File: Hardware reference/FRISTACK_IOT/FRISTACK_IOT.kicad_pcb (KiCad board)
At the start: 2 copper layers, 51 x 51 mm, 66 parts, among them J1 MEM2075-00-140-01-A, J2 Conn_01x02_Pin, J3 Conn_01x13_Socket, J4 Conn_01x13_Socket, U1 TPS62840DLCR, U2 ESP32-C6-MINI-1-H4, U3 SN65HVD232, Y1 32.768 kHz

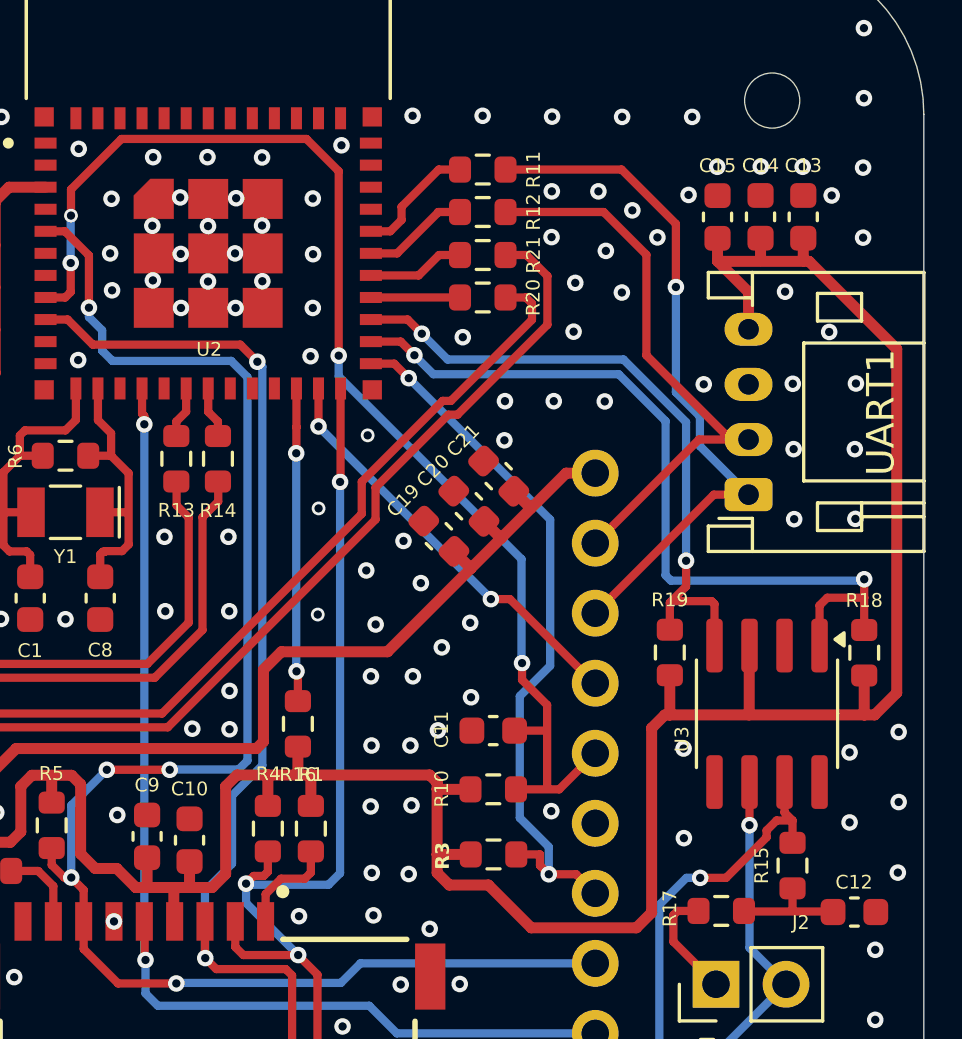
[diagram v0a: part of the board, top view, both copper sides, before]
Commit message: Added USBSwitch to Core and added first version of Compatibility
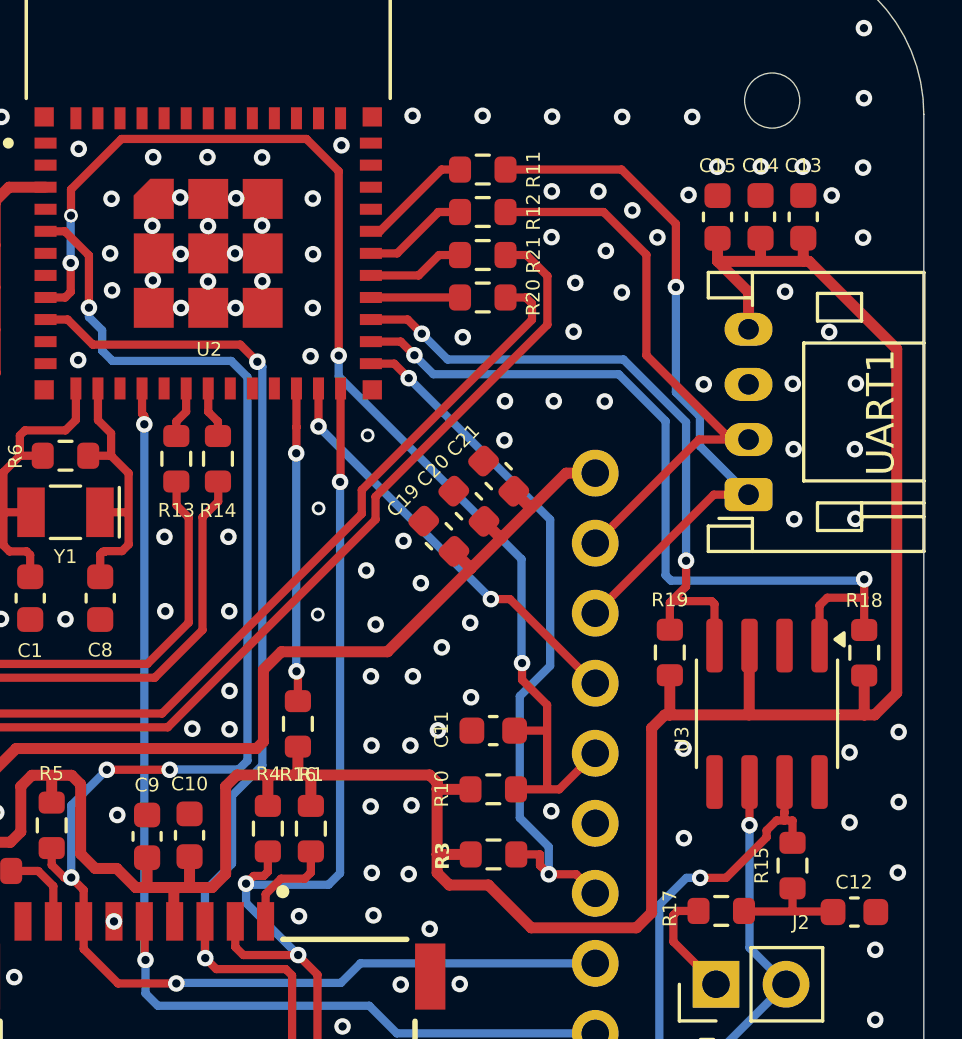
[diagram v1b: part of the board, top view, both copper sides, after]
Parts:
- moved C10 0.18 mm to (161.3, 98.1)
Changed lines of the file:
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@@
 			(psa4output no)
 			(plot_black_and_white yes)
-			(plotinvisibletext yes)
 			(sketchpadsonfab no)
 			(plotpadnumbers no)
@@
 	(footprint "Capacitor_SMD:C_0603_1608Metric"
 		(layer "F.Cu")
-		(at 161.28 98.255 90)
+		(at 161.28 98.075 90)
 		(descr "Capacitor SMD 0603 (1608 Metric), square (rectangular) end terminal, IPC_7351 nominal, (Body size source: IPC-SM-782 page 76, https://www.pcb-3d.com/wordpress/wp-content/uploads/ipc-sm-782a_amendment_1_and_2.pdf), generated with kicad-footprint-generator")
 		(tags "capacitor")
@@
 	)
 	(segment
-		(start 145.455 97.715)
-		(end 145.44 97.7)
-		(width 0.3)
-		(layer "F.Cu")
-		(net 12)
-	)
-	(segment
-		(start 170.76 82.32)
-		(end 173.7 79.38)
+		(start 147.945476 99.785349)
+		(end 154.071826 93.659)
 		(width 0.3)
 		(layer "F.Cu")
@@
 	)
 	(segment
-		(start 154.071826 93.659)
-		(end 160.28248 93.659)
+		(start 145.455 97.715)
+		(end 145.44 97.7)
 		(width 0.3)
 		(layer "F.Cu")
@@
 	)
 	(segment
-		(start 173.48 78.57)
-		(end 172.74 78.57)
+		(start 167.52574 86.41574)
+		(end 167.52574 85.55426)
 		(width 0.3)
 		(layer "F.Cu")
@@
 	)
 	(segment
-		(start 145.44 90.76)
-		(end 145.05 90.37)
-		(width 0.3)
-		(layer "F.Cu")
-		(net 12)
-	)
-	(segment
-		(start 167.52574 86.41574)
-		(end 167.52574 85.25426)
+		(start 167.52574 85.55426)
+		(end 173.7 79.38)
 		(width 0.3)
 		(layer "F.Cu")
@@
 	)
 	(segment
-		(start 147.945476 99.785349)
-		(end 154.071826 93.659)
+		(start 145.44 90.76)
+		(end 145.05 90.37)
 		(width 0.3)
 		(layer "F.Cu")
@@
 	)
 	(segment
-		(start 170.46 82.32)
-		(end 170.76 82.32)
+		(start 154.071826 93.659)
+		(end 160.28248 93.659)
 		(width 0.3)
 		(layer "F.Cu")
@@
 	)
 	(segment
-		(start 145.455 97.715)
-		(end 145.405 97.765)
+		(start 173.48 78.57)
+		(end 172.74 78.57)
 		(width 0.3)
 		(layer "F.Cu")
@@
 	)
 	(segment
-		(start 147.945476 100.18175)
-		(end 147.945476 99.785349)
+		(start 173.7 79.38)
+		(end 173.7 78.79)
 		(width 0.3)
 		(layer "F.Cu")
@@
 	)
 	(segment
-		(start 167.52574 85.25426)
-		(end 170.46 82.32)
+		(start 145.455 97.715)
+		(end 145.405 97.765)
 		(width 0.3)
 		(layer "F.Cu")
@@
 	)
 	(segment
-		(start 173.7 79.38)
-		(end 173.7 78.79)
+		(start 147.945476 100.18175)
+		(end 147.945476 99.785349)
 		(width 0.3)
 		(layer "F.Cu")
@@
 	)
 	(segment
-		(start 146.45 102.72)
-		(end 146.25 102.52)
+		(start 160.490001 94.16)
+		(end 168.02674 86.62326)
 		(width 0.3)
 		(layer "F.Cu")
@@
 	)
 	(segment
-		(start 170.999 82.821)
-		(end 174.26 79.56)
+		(start 146.45 102.72)
+		(end 146.25 102.52)
 		(width 0.3)
 		(layer "F.Cu")
@@
 	)
 	(segment
-		(start 168.02674 85.46178)
-		(end 170.66752 82.821)
+		(start 149.54 101.127226)
+		(end 149.54 98.899346)
 		(width 0.3)
 		(layer "F.Cu")
@@
 	)
 	(segment
-		(start 173.5 77.03)
-		(end 172.74 77.03)
-		(width 0.3)
-		(layer "F.Cu")
-		(net 18)
-	)
-	(segment
 		(start 147.945476 102.72175)
 		(end 147.943726 102.72)
@@
 	)
 	(segment
-		(start 168.02674 86.62326)
-		(end 168.02674 85.46178)
-		(width 0.3)
-		(layer "F.Cu")
-		(net 18)
-	)
-	(segment
-		(start 147.945476 102.72175)
-		(end 149.54 101.127226)
+		(start 154.279348 94.160001)
+		(end 160.490001 94.16)
 		(width 0.3)
 		(layer "F.Cu")
@@
 	)
 	(segment
-		(start 170.66752 82.821)
-		(end 170.999 82.821)
+		(start 146.44 102.71)
+		(end 146.44 89.59)
 		(width 0.3)
 		(layer "F.Cu")
@@
 	)
 	(segment
-		(start 149.54 101.127226)
-		(end 149.54 98.899346)
+		(start 149.54 98.899346)
+		(end 154.279345 94.160001)
 		(width 0.3)
 		(layer "F.Cu")
@@
 	)
 	(segment
-		(start 146.44 102.71)
-		(end 146.44 89.59)
+		(start 146.44 89.59)
+		(end 145.19 88.34)
 		(width 0.3)
 		(layer "F.Cu")
@@
 	)
 	(segment
-		(start 174.26 77.79)
-		(end 173.5 77.03)
+		(start 143.26155 88.34)
+		(end 143.23155 88.37)
 		(width 0.3)
 		(layer "F.Cu")
@@
 	)
 	(segment
-		(start 146.44 89.59)
-		(end 145.19 88.34)
+		(start 168.02674 85.79326)
+		(end 174.26 79.56)
 		(width 0.3)
 		(layer "F.Cu")
@@
 	)
 	(segment
-		(start 143.26155 88.34)
-		(end 143.23155 88.37)
+		(start 168.02674 86.62326)
+		(end 168.02674 85.79326)
 		(width 0.3)
 		(layer "F.Cu")
@@
 	)
 	(segment
-		(start 160.490001 94.16)
-		(end 168.02674 86.62326)
+		(start 174.26 77.79)
+		(end 173.5 77.03)
 		(width 0.3)
 		(layer "F.Cu")
@@
 	)
 	(segment
-		(start 149.54 98.899346)
-		(end 154.279345 94.160001)
+		(start 154.279345 94.160001)
+		(end 154.279349 94.16)
 		(width 0.3)
 		(layer "F.Cu")
@@
 	)
 	(segment
-		(start 154.279348 94.160001)
-		(end 160.490001 94.16)
+		(start 173.5 77.03)
+		(end 172.74 77.03)
 		(width 0.3)
 		(layer "F.Cu")
@@
 	)
 	(segment
-		(start 154.279345 94.160001)
-		(end 154.279349 94.16)
+		(start 147.945476 102.72175)
+		(end 149.54 101.127226)
 		(width 0.3)
 		(layer "F.Cu")
@@
 	)
 	(segment
-		(start 182.86 97.25)
-		(end 182.86 96.145)
-		(width 0.3)
-		(layer "F.Cu")
-		(net 20)
-	)
-	(segment
 		(start 182.57 97.54)
 		(end 182.21 97.9)
@@
 	)
 	(segment
+		(start 182.85 97.54)
+		(end 182.85 97.26)
+		(width 0.3)
+		(layer "F.Cu")
+		(net 20)
+	)
+	(segment
 		(start 182.21 98.15)
 		(end 180.74 99.62)
@@
 	)
 	(segment
+		(start 182.85 97.26)
+		(end 182.86 97.25)
+		(width 0.3)
+		(layer "F.Cu")
+		(net 20)
+	)
+	(segment
 		(start 180.74 99.62)
 		(end 179.8 99.62)
@@
 	)
 	(segment
-		(start 178.73 106.37)
-		(end 180.275 106.37)
+		(start 182.86 97.25)
+		(end 182.86 96.145)
 		(width 0.3)
 		(layer "F.Cu")
@@
 	)
 	(segment
-		(start 183.15 97.54)
-		(end 182.86 97.25)
+		(start 178.73 106.37)
+		(end 180.275 106.37)
 		(width 0.3)
 		(layer "F.Cu")
@@
 	)
 	(segment
-		(start 170.32 73.93)
-		(end 168.97 75.28)
-		(width 0.3)
-		(layer "F.Cu")
-		(net 29)
-	)
-	(segment
-		(start 168.5575 76.17)
+		(start 168.18 76.17)
 		(end 167.8575 76.17)
 		(width 0.3)
@@
 	)
 	(segment
-		(start 168.97 75.7575)
-		(end 168.5575 76.17)
-		(width 0.3)
-		(layer "F.Cu")
-		(net 29)
-	)
-	(segment
-		(start 168.97 75.28)
-		(end 168.97 75.7575)
+		(start 171.09 73.93)
+		(end 170.42 73.93)
 		(width 0.3)
 		(layer "F.Cu")
@@
 	)
 	(segment
-		(start 171.09 73.93)
-		(end 170.32 73.93)
+		(start 170.42 73.93)
+		(end 168.18 76.17)
 		(width 0.3)
 		(layer "F.Cu")
@@
 	)
 	(group ""
-		(members "2791a95b-42e5-4102-ae3b-9cf65cbf0bcc" "2dfbaade-4923-48d9-aa6f-134091588e89"
-			"31310593-05bf-4365-994b-4dc35888f404" "4e13a2d6-105e-4052-ba09-1d7e4f1ce143"
-			"88e18c7d-14a1-43d4-ac31-33f592af2c9c" "ee10c7a8-357f-46bc-b261-197f884fdc5f"
+		(members "2791a95b-42e5-4102-ae3b-9cf65cbf0bcc" "88e18c7d-14a1-43d4-ac31-33f592af2c9c"
+			"ee10c7a8-357f-46bc-b261-197f884fdc5f"
 		)
 	)

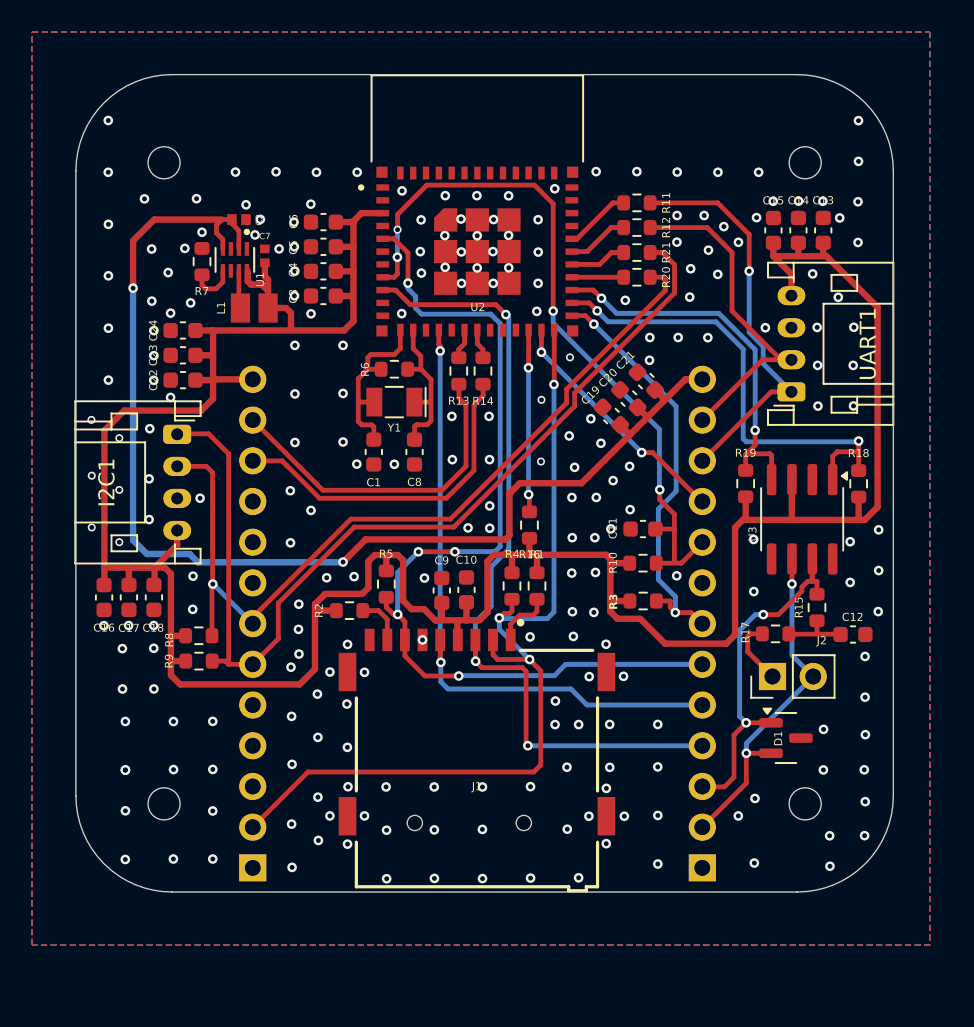
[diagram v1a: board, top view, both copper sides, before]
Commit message: review and new BATTERY board
IOT - changed twai termination from header to switch option, new holes , added power planes
SENSOR NODE - new holes and back silk text
CORE - vertical twai termination header changed to horizontal
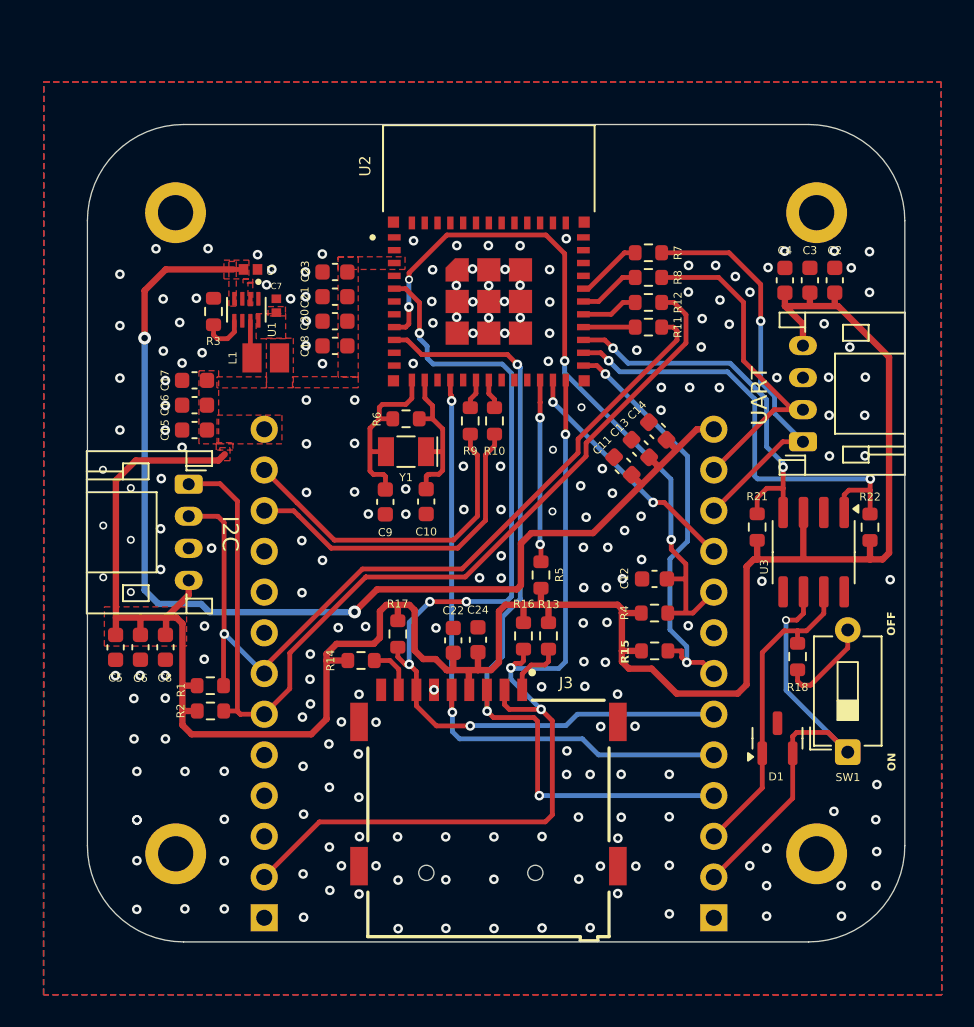
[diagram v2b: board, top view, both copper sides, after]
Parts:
- removed C19: 2.2uF, Capacitor_SMD:C_0603_1608Metric
- removed I2C1, UART1: Conn_01x04_Pin, Connector_JST:JST_PH_S4B-PH-K_1x04_P2.00mm_Horizontal
- removed J4: Conn_01x13_Socket, Connector_PinSocket_2.54mm:PinSocket_1x13_P2.54mm_Vertical
- removed R19: 4K7, Resistor_SMD:R_0603_1608Metric
- removed R20: 22, Resistor_SMD:R_0603_1608Metric
- removed REF** (x4): MountingHole_2mm, MountingHole:MountingHole_2mm
- removed REF**: KiCad-Logo2_5mm_SilkScreen, Symbol:KiCad-Logo2_5mm_SilkScreen
- removed REF**: OSHW-Logo_5.7x6mm_SilkScreen, Symbol:OSHW-Logo_5.7x6mm_SilkScreen
- added ?: , clipboard:622c10b6-db75-403c-84c1-658ef0b72b12, F.Cu at (143.1, 112.6)
- added ?: , clipboard:622c10b6-db75-403c-84c1-658ef0b72b12, F.Cu at (183.1, 112.6)
- added ?: , clipboard:622c10b6-db75-403c-84c1-658ef0b72b12, F.Cu at (183.1, 72.6)
- added ?: , clipboard:622c10b6-db75-403c-84c1-658ef0b72b12, F.Cu at (143.1, 72.6)
- added I2C: Conn_01x04_Pin, Connector_JST:JST_PH_S4B-PH-K_1x04_P2.00mm_Horizontal, F.Cu at (143.9, 91.5)
- added R22: 4K7, Resistor_SMD:R_0603_1608Metric, F.Cu at (186.5, 94.2)
- added SW1: SW_DIP_x01, Button_Switch_THT:SW_DIP_SPSTx01_Slide_6.7x4.1mm_W7.62mm_P2.54mm_LowProfile, F.Cu at (185.1, 108.2)
- added UART: Conn_01x04_Pin, Connector_JST:JST_PH_S4B-PH-K_1x04_P2.00mm_Horizontal, F.Cu at (182.3, 88.8)
- C1: value 15pF -> 4.7uF; footprint Capacitor_SMD:C_0603_1608Metric -> GRM155R61A475MEAAD:CAPC1005X65N
- C10: value 100nF -> 15pF
- C11: value 0.1uF -> 2.2uF
- C12: value 4.7nF -> 0.1uF
- C13, C16: value 2.2uF -> 100nF
- C14, C17, C4: value 100nF -> 1nF
- C15, C5: value 1nF -> 2.2uF
- C18: value 1nF -> 22uF
- C2: value 4.7uF -> 2.2uF; footprint GRM155R61A475MEAAD:CAPC1005X65N -> Capacitor_SMD:C_0603_1608Metric
- C22: value 2.2uF -> 10uF
- C23: value 100nF -> 100pF
- C24: value 1nF -> 100nF
- C3: value 22uF -> 100nF
- C6: value 100pF -> 100nF
- C8: value 15pF -> 1nF
- C9: value 10uF -> 15pF
- J1: value MEM2075-00-140-01-A -> Conn_01x13_Socket; footprint MEM2075-00-140-01-A:GCT_MEM2075-00-140-01-A -> Connector_PinSocket_2.54mm:PinSocket_1x13_P2.54mm_Vertical; moved to B.Cu
- J2: value Conn_01x02_Pin -> Conn_01x13_Socket; footprint Connector_PinHeader_2.54mm:PinHeader_1x02_P2.54mm_Vertical -> Connector_PinSocket_2.54mm:PinSocket_1x13_P2.54mm_Vertical; moved to B.Cu
- J3: value Conn_01x13_Socket -> MEM2075-00-140-01-A; footprint Connector_PinSocket_2.54mm:PinSocket_1x13_P2.54mm_Vertical -> MEM2075-00-140-01-A:GCT_MEM2075-00-140-01-A; moved to F.Cu
- R1, R2: value 10K -> 4K7
- R10: value 10K -> 22
- R13, R14: value 22 -> 10K
- R15: value 60 -> 22K
- R16: value 10K -> 22K
- R17: value 60 -> 47K
- R18: value 4K7 -> 120
- R21: value 22 -> 4K7
- R3: value 22K -> 267k
- R4: value 22K -> 10K
- R5: value 47K -> 10K
- R7: value 267k -> 22
- R8, R9: value 4K7 -> 22
- moved C15 38.2 mm to (144.3, 88.1), turned to 180 degrees
- moved C2 37.4 mm to (184.3, 78.8), turned to 90 degrees
- moved R8 35.9 mm to (172.6, 78.6)
- moved R3 32.3 mm to (145.5, 80.7), turned to 90 degrees
- moved C3 30.4 mm to (182.7, 78.8), turned to 90 degrees
- moved C6 28.9 mm to (140.9, 101.7), turned to -90 degrees
- moved C4 28.8 mm to (181.1, 78.8), turned to 90 degrees
- moved C5 28.2 mm to (139.4, 101.7), turned to -90 degrees
- moved R7 27.9 mm to (172.6, 77.0), turned to 180 degrees
- moved C24 26.7 mm to (162.0, 101.2), turned to 90 degrees
- moved R17 23.6 mm to (157.0, 100.8), turned to 90 degrees
- moved C22 23.4 mm to (160.5, 101.2), turned to 90 degrees
- moved R9 22.6 mm to (161.5, 87.5), turned to 90 degrees
- moved R1 21.3 mm to (145.3, 104.1), turned to 180 degrees
- moved C21 20.1 mm to (153.1, 79.8), turned to 180 degrees
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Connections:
- C1 pad 1: GND -> +5V
- C1 pad 2: XTAL_32K_P -> GND
- C10 pad 1: ESP_PWR -> GND
- C10 pad 2: GND -> XTAL_32K_N
- C11 pad 1: FLASH_RST -> +5V
- C12 pad 1: Net-(C12-Pad1) -> FLASH_RST
- C13 pad 1: ESP_PWR -> +5V
- C14 pad 1: ESP_PWR -> +5V
- C2 pad 1: +5V -> ESP_PWR
- C20 pad 1: +5V -> ESP_PWR
- C21 pad 1: +5V -> ESP_PWR
- C8 pad 1: GND -> ESP_PWR
- C8 pad 2: XTAL_32K_N -> GND
- C9 pad 1: ESP_PWR -> GND
- C9 pad 2: GND -> XTAL_32K_P
- J2 pad 1: Net-(J2-Pin_1) -> GND
- R1 pad 1: SD_DAT_2 -> SDA
- R10 pad 1: ESP_PWR -> USB_P_HD
- R10 pad 2: FLASH_RST -> Net-(U2-IO13)
- R11 pad 1: UART0_TX -> SDA
- R11 pad 2: Net-(U2-TXD0) -> Net-(U2-IO22)
- R12 pad 1: UART0_RX -> SCL
- R12 pad 2: Net-(U2-RXD0) -> Net-(U2-IO23)
- R13 pad 1: USB_N_HD -> SD_DAT_2
- R13 pad 2: Net-(U2-IO12) -> ESP_PWR
- R14 pad 1: USB_P_HD -> SD_DAT_1
- R14 pad 2: Net-(U2-IO13) -> ESP_PWR
- R15 pad 1: CAN_H -> CS
- R15 pad 2: Net-(C12-Pad1) -> ESP_PWR
- R16 pad 1: Net-(U2-IO8) -> SD_CS
- R17 pad 1: Net-(C12-Pad1) -> MISO
- R17 pad 2: Net-(J2-Pin_1) -> ESP_PWR
- R18 pad 1: CAN_D -> CAN_H
- R18 pad 2: ESP_PWR -> Net-(R23-Pad2)
- R2 pad 1: SD_DAT_1 -> SCL
- R21 pad 1: SCL -> ESP_PWR
- R21 pad 2: Net-(U2-IO23) -> CAN_R
- R3 pad 1: CS -> Net-(U1-VSET)
- R3 pad 2: ESP_PWR -> GND
- R4 pad 1: SD_CS -> ESP_PWR
- R4 pad 2: ESP_PWR -> FLASH_RST
- R5 pad 1: MISO -> Net-(U2-IO8)
- R7 pad 1: Net-(U1-VSET) -> UART0_TX
- R7 pad 2: GND -> Net-(U2-TXD0)
- R8 pad 1: SDA -> UART0_RX
- R8 pad 2: ESP_PWR -> Net-(U2-RXD0)
- R9 pad 1: SCL -> USB_N_HD
- R9 pad 2: ESP_PWR -> Net-(U2-IO12)
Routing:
- net ESP_PWR: track 186.0 -> 146.8 mm
- net Net-(R23-Pad2): track 0.00 -> 6.02 mm
- net CAN_L: track 21.7 -> 27.3 mm, vias 2 -> 1
- net +5V: track 74.5 -> 70.4 mm
- net Net-(J2-Pin_1): track 4.12 -> 0.00 mm
- net Net-(C12-Pad1): track 4.10 -> 0.00 mm
- net CAN_H: track 21.9 -> 19.7 mm, vias 2 -> 0
- net CAN_D: track 29.8 -> 29.0 mm
- net GND: vias 241 -> 219
- added copper zone on F.Cu, net +5V
- added copper zone on B.Cu, net CAN_D
- added copper zone on F.Cu, net CAN_D
- added copper zone on F.Cu, net ESP_PWR
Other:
- board text added: "+5V/BAT"
- board text added: "BAT"
- board text added: "Designed by Andrej Šimkovič & Marián Bobček 2025"
- board text added: "OFF"
- board text added: "ON"
- board text removed: "+5V"
- board text removed: "GPIO14"
